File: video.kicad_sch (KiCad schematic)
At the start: 0 parts

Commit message: add video padding circuit
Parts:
- added C46: 180pF, Capacitor_THT:C_Disc_D3.0mm_W2.0mm_P2.50mm, symbol Device:C_Small
- added C47, C71: 100pF, Capacitor_THT:C_Disc_D3.0mm_W2.0mm_P2.50mm, symbol Device:C_Small
- added C73, C99: 180pF, Capacitor_THT:C_Disc_D4.7mm_W2.5mm_P5.00mm, symbol Device:C_Small
- added IC11: MC14053, Package_DIP:DIP-16_W7.62mm, symbol vdg:MC14053
- added IC14: 74LS86AN, Package_DIP:DIP-14_W7.62mm, symbol 74xx:74LS86
- added IC21: 74LS74, Package_DIP:DIP-14_W7.62mm, symbol 74xx:74LS74
- added IC22: 74LS00N, Package_DIP:DIP-14_W7.62mm, symbol 74xx:74LS00
- added IC23: 74ALS74N, Package_DIP:DIP-14_W7.62mm, symbol 74xx:74LS74
- added IC27: 74LS20N, Package_DIP:DIP-14_W7.62mm, symbol 74xx:74LS20
- added IC28, IC29: 74LS393N, Package_DIP:DIP-14_W7.62mm, symbol 74xx:74LS393
- added IC30: 74LS32N, Package_DIP:DIP-14_W7.62mm, symbol 74xx:74LS32
- added IC32: 74LS390, Package_DIP:DIP-16_W7.62mm, symbol 74xx:74LS390
- added IC44: MC3346, Package_DIP:DIP-14_W7.62mm, symbol vdg:MC3346
- added L5, L99: 3.3uH, Inductor_THT:L_Axial_L7.0mm_D3.3mm_P12.70mm_Horizontal_Fastron_MICC, symbol Device:FerriteBead_Small
- added R33: 1K8, Dragon:R_Axial_DIN0309_L9.0mm_D2.5mm_P12.70mm_Horizontal, symbol Device:R_Small
- added R34: 8K2, Dragon:R_Axial_DIN0309_L9.0mm_D2.5mm_P12.70mm_Horizontal, symbol Device:R_Small
- added R35, R92, R94, R99: 12K, Dragon:R_Axial_DIN0309_L9.0mm_D2.5mm_P12.70mm_Horizontal, symbol Device:R_Small
- added U1: LINE_PULSE_DIAGRAM, symbol Dragon32_MKII:LINE_PULSE_DIAGRAM
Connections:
- new net: C46.1, IC30.11, IC30.4
- new net: IC29.11 (Q0), IC30.12
- new net: IC27.12, IC29.10 (Q1), IC30.13
- new net: IC14.6, IC23.11 (C)
- new net: IC14.8, IC23.12 (D)
- new net: IC22.12, IC23.9 (Q)
- new net: IC27.9, IC29.8 (Q3), IC30.10
- new net: C47.1, IC30.5, IC30.8
- new net: IC27.10, IC29.9 (Q2), IC30.9
- new net: IC32.12 (~{CP1}), IC32.7 (Q3)
- new net: C99.2, L99.1
- new net: IC14.11, IC27.1, IC27.2
- new net: IC27.4, IC28.11 (Q0)
- new net: IC27.5, IC28.13 (CP), IC28.6 (Q3)
- new net: IC14.10, IC32.13 (Q0)
- new net: IC32.15 (~{CP0}), IC32.9 (Q3)
- new net: IC22.4, IC22.5, IC27.8
- new net: IC44.5, IC44.8
- new net: IC23.2 (D), IC23.6 (~{Q})
- new net: IC27.13, IC29.5 (Q2)
- new net: IC22.3, R35.2
- new net +5V: IC11.16 (VDD), IC14.13, IC14.14 (VCC), IC14.4, IC21.1 (~{R}), IC21.10 (~{S}), IC21.13 (~{R}), IC21.14 (VCC), IC22.14 (VCC), IC23.1 (~{R}), IC23.10 (~{S}), IC23.13 (~{R}), IC23.14 (VCC), IC23.4 (~{S}), IC27.14 (VCC), IC28.7 (GND), IC29.14 (VCC), IC30.14 (VCC), IC32.16 (VCC), IC44.1, R34.2
- new net CHROME CONTROL: IC23.5 (Q)
- new net CLK: IC22.11
- new net E: IC21.11 (C), IC21.3 (C)
- new net FS': IC14.9, IC27.6
- new net GND: C46.2, C47.2, C71.2, IC11.7 (VEE), IC11.8 (VSS), IC14.7 (GND), IC21.2 (D), IC21.7 (GND), IC22.7 (GND), IC23.7 (GND), IC27.7 (GND), IC28.14 (VCC), IC29.7 (GND), IC30.1, IC30.2, IC30.7 (GND), IC32.14 (MR), IC32.2 (MR), IC32.8 (GND), L99.2, R33.1
- new net LINE PULSE: R33.2, R34.1, R35.1
- new net LINE PULSES: IC14.2, IC22.1, IC22.2, IC30.6, IC32.4 (~{CP1})
- new net LUM CONTROL: IC22.9, IC23.8 (~{Q})
- new net VCLK: IC14.5, IC22.10, IC22.13
- new net u1: IC21.5 (Q), IC22.6, IC29.12 (MR), IC29.2 (MR)
- new net u2: C73.2, IC44.2
- new net u3: IC44.3, R94.2
- new net u4: IC44.4, R92.2
- new net u5: IC44.6, L5.1
- new net u6: C71.1, IC11.14 (X), IC44.10, IC44.13, IC44.7, R99.1
- new net u7: IC44.12
- new net u8: C99.1, IC44.14
- new net ~{FS}: IC14.12, IC21.4 (~{S}), IC28.12 (MR), IC28.2 (MR)
- new net ~{HS}: IC14.1, IC21.12 (D), IC28.1 (CP)
- new net ~{NHS}: IC14.3, IC21.9 (Q), IC23.3 (C)
- new net ~{VCLK}: IC22.8, IC29.1 (CP)
- new net ~{VCLK}/16: IC29.13 (CP), IC29.6 (Q3)
- no-connect marks 0 -> 17
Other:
- note added: "24 LINE DELAY"
- note added: "DIVIDE BY 50"
- note added: "DIVIDE VCLK BY 228 TO CREATE LINE PULSE FREQUENCY"
- note added: "HSYNC DIVIDED BY 2"
- note added: "OUTPUT LOW ON COUNT 0-15 LINE PULSE WIDTH = 4.5us"
- note added: "STEER VCLK TO VDG OR LINE PULSE CIRCUIT"

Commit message: video circuit tracing
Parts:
- added C53, C54, C55, C56: 100nF, Capacitor_THT:C_Disc_D4.3mm_W1.9mm_P5.00mm, symbol Device:C_Small
- added C60: 180pF, Capacitor_THT:C_Disc_D3.0mm_W2.0mm_P2.50mm, symbol Device:C_Small
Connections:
- net +5V: now also IC14.10, IC14.5, IC28.14 (VCC), C53.2, C54.2, C55.2, C56.2; no longer IC14.13, IC14.4, IC28.7 (GND)
- net FS': now also IC14.12; no longer IC14.9
- net GND: now also IC28.7 (GND), C53.1, C54.1, C55.1, C56.1, C60.2; no longer IC28.14 (VCC)
- net LINE PULSE: now also IC11.3 (Z1)
- net LINE PULSES: now also C60.1
- net LUM CONTROL: now also IC11.9 (C)
- net VCLK: now also IC14.4; no longer IC14.5
- net ~{FS}: now also IC14.9; no longer IC14.12
- net at IC23.12 (D): now also IC14.11; no longer IC14.8
- net LUMA': now reaches IC11.4 (Z)
- net LUM: now reaches IC11.5 (Z0)
- net at IC27.1, IC27.2: now also IC14.8; no longer IC14.11
- net at IC32.13 (Q0): now also IC14.13; no longer IC14.10

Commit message: FM generator routing
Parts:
- added C49: 100nF, Capacitor_THT:C_Disc_D4.3mm_W1.9mm_P5.00mm, symbol Device:C_Small
- added C67, C72, C75, C76: 100pF, Capacitor_THT:C_Disc_D3.0mm_W2.0mm_P2.50mm, symbol Device:C_Small
- added C74: 100nF, Capacitor_THT:C_Disc_D4.7mm_W2.5mm_P5.00mm, symbol Device:C_Small
- added C98: 33nF, Capacitor_THT:C_Disc_D3.0mm_W2.0mm_P2.50mm, symbol Device:C_Small
- added DL1: 390ns 1K1, Dragon:Delay_Line-V9663, symbol Device:DelayLine
- added L4: 22uH, Inductor_THT:L_Axial_L9.5mm_D4.0mm_P15.24mm_Horizontal_Fastron_SMCC, symbol Device:FerriteBead_Small
- added L6, L7: 10.7MHz, Dragon:TOKO_RCL_10K, symbol vdg:TOKO_Variable_Inductor
- added R100, R91, R93: 6K5, Dragon:R_Axial_DIN0309_L9.0mm_D2.5mm_P12.70mm_Horizontal, symbol Device:R_Small
- added R77: 1200uH, Dragon:R_Axial_DIN0309_L9.0mm_D2.5mm_P12.70mm_Horizontal, symbol Device:R_Small
- added R86, R96: 47K, Dragon:R_Axial_DIN0309_L9.0mm_D2.5mm_P12.70mm_Horizontal, symbol Device:R_Small
- added R95, R98: 470uH, Dragon:R_Axial_DIN0309_L9.0mm_D2.5mm_P12.70mm_Horizontal, symbol Device:R_Small
- added R97: 270R, Dragon:R_Axial_DIN0309_L9.0mm_D2.5mm_P12.70mm_Horizontal, symbol Device:R_Small
- C73: value 180pF -> 100nF
- L5: footprint Inductor_THT:L_Axial_L7.0mm_D3.3mm_P12.70mm_Horizontal_Fastron_MICC -> Inductor_THT:L_Axial_L9.5mm_D4.0mm_P15.24mm_Horizontal_Fastron_SMCC
- R92: value 12K -> 6K5
- R94, R99: value 12K -> 1K6
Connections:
- net +5V: now also IC44.11, C49.2, L6.1
- net CHROME CONTROL: now also IC11.10 (B)
- net E: now also IC30.2
- net GND: now also C46.1, C47.1, IC11.6 (INHIBIT), R94.1, R99.2, C49.1, C74.1, DL1.3 (COMMUN), L6.5 (GND), L7.5 (GND), R100.2, R91.1; no longer C46.2, C47.2, C71.2, IC30.1, IC30.2
- net u2: now also C72.1
- net u4: now also C74.2, R93.2, R95.1
- net u6: no longer IC11.14 (X)
- net ~{NHS}: no longer IC14.3, IC23.3 (C)
- net at IC30.11, IC30.4: now also C46.2; no longer C46.1
- net at C73.1: now also R92.1
- net at IC30.5, IC30.8: now also C47.2; no longer C47.1
- net C1: now reaches IC11.2 (Y0)
- net C1: now also R86.2
- net DA0': now reaches IC30.3
- net u9: now reaches IC44.5, IC44.8
- net u9: now also C71.2, C72.2, C75.2, L6.3
- net u10: now reaches IC44.9
- net u10: now also IC11.14 (X)
- net u1: no longer names the net of IC22.6, IC29.12 (MR), IC29.2 (MR)
- net u1: no longer IC21.5 (Q)
- new net: C67.1, R86.1
- new net: C76.2, R100.1
- new net: C98.1, R77.1, R95.2
- new net: R93.1, R96.1
- new net: L7.1, R98.1
- new net: C76.1, L7.3
- new net: C98.2, L4.2
- new net: C75.1, R91.2
- new net: IC14.3, IC23.3 (C)
- new net DA0: IC30.1
- new net ~{NFS}: IC21.5 (Q)
- no-connect marks 17 -> 19
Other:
- moved on the sheet: C71, C73, C99, IC11, IC14A, IC21A, IC21B, IC23A, IC28B, IC30A, L5, L99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

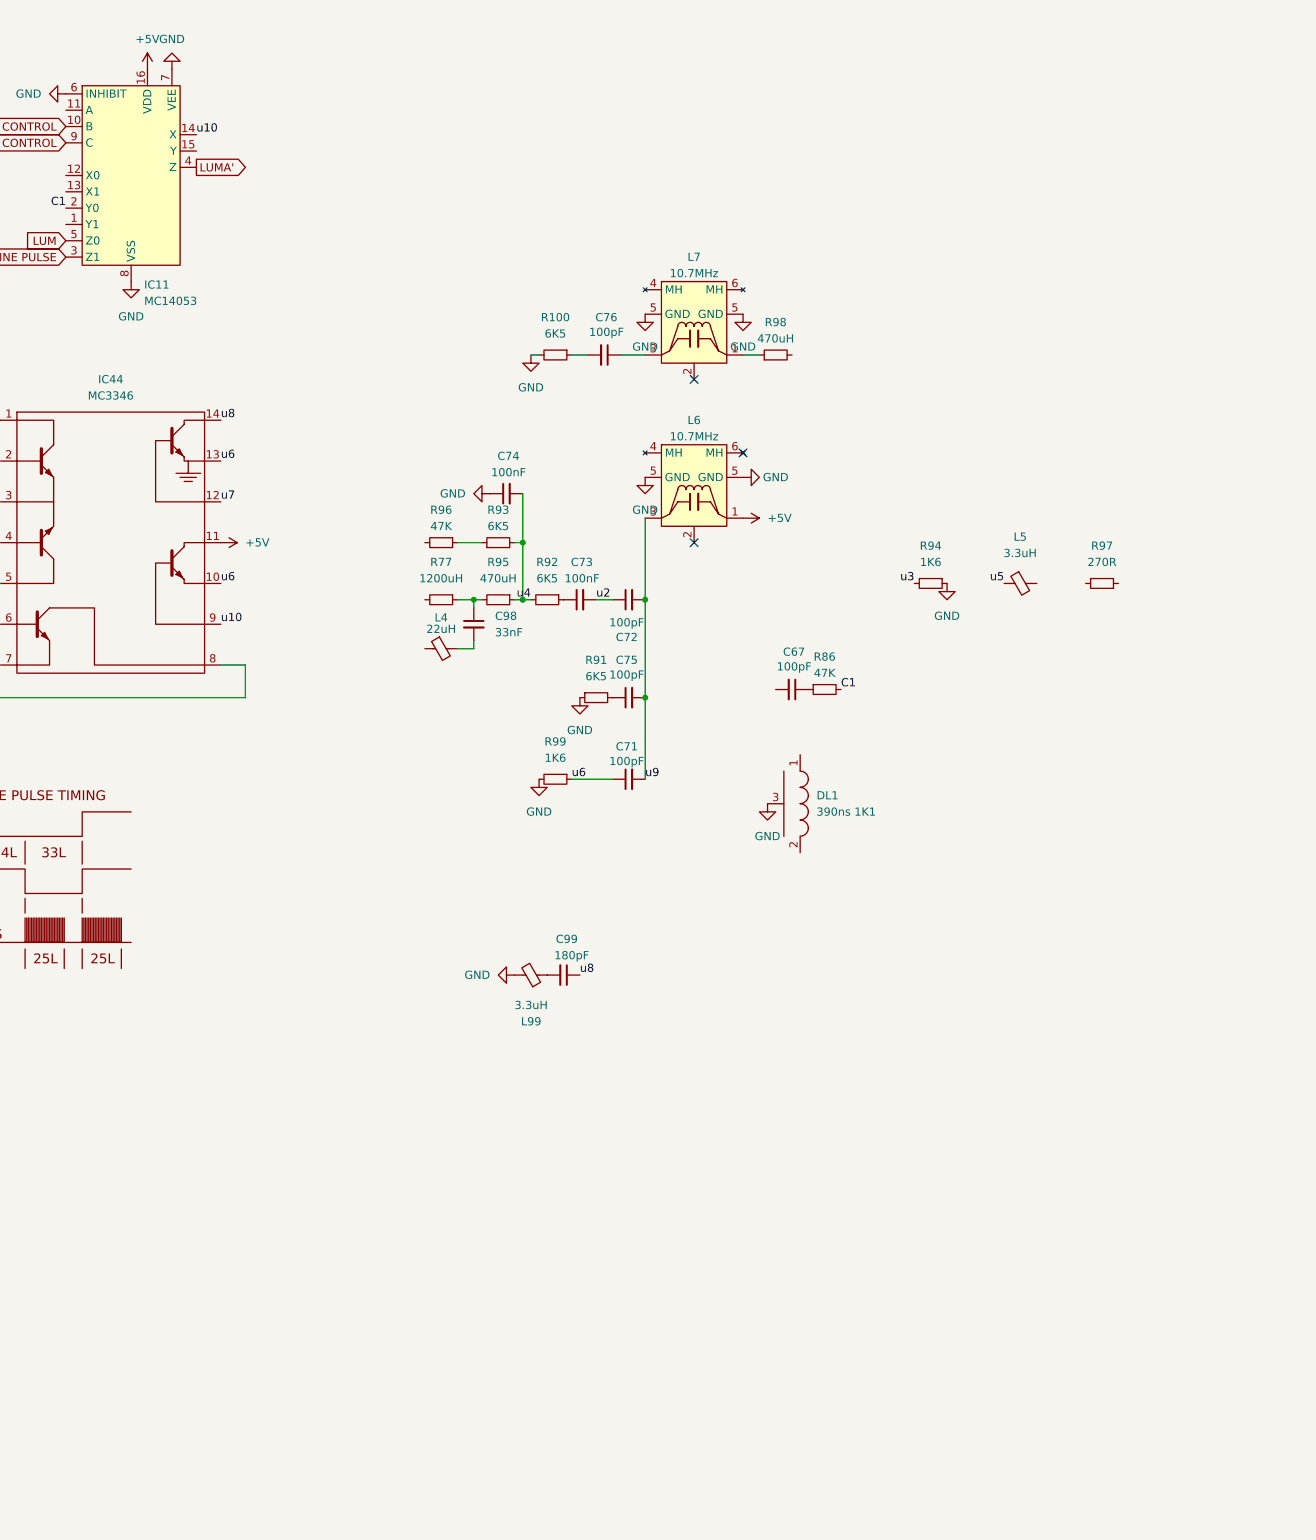
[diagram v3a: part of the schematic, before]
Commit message: complete physical layout
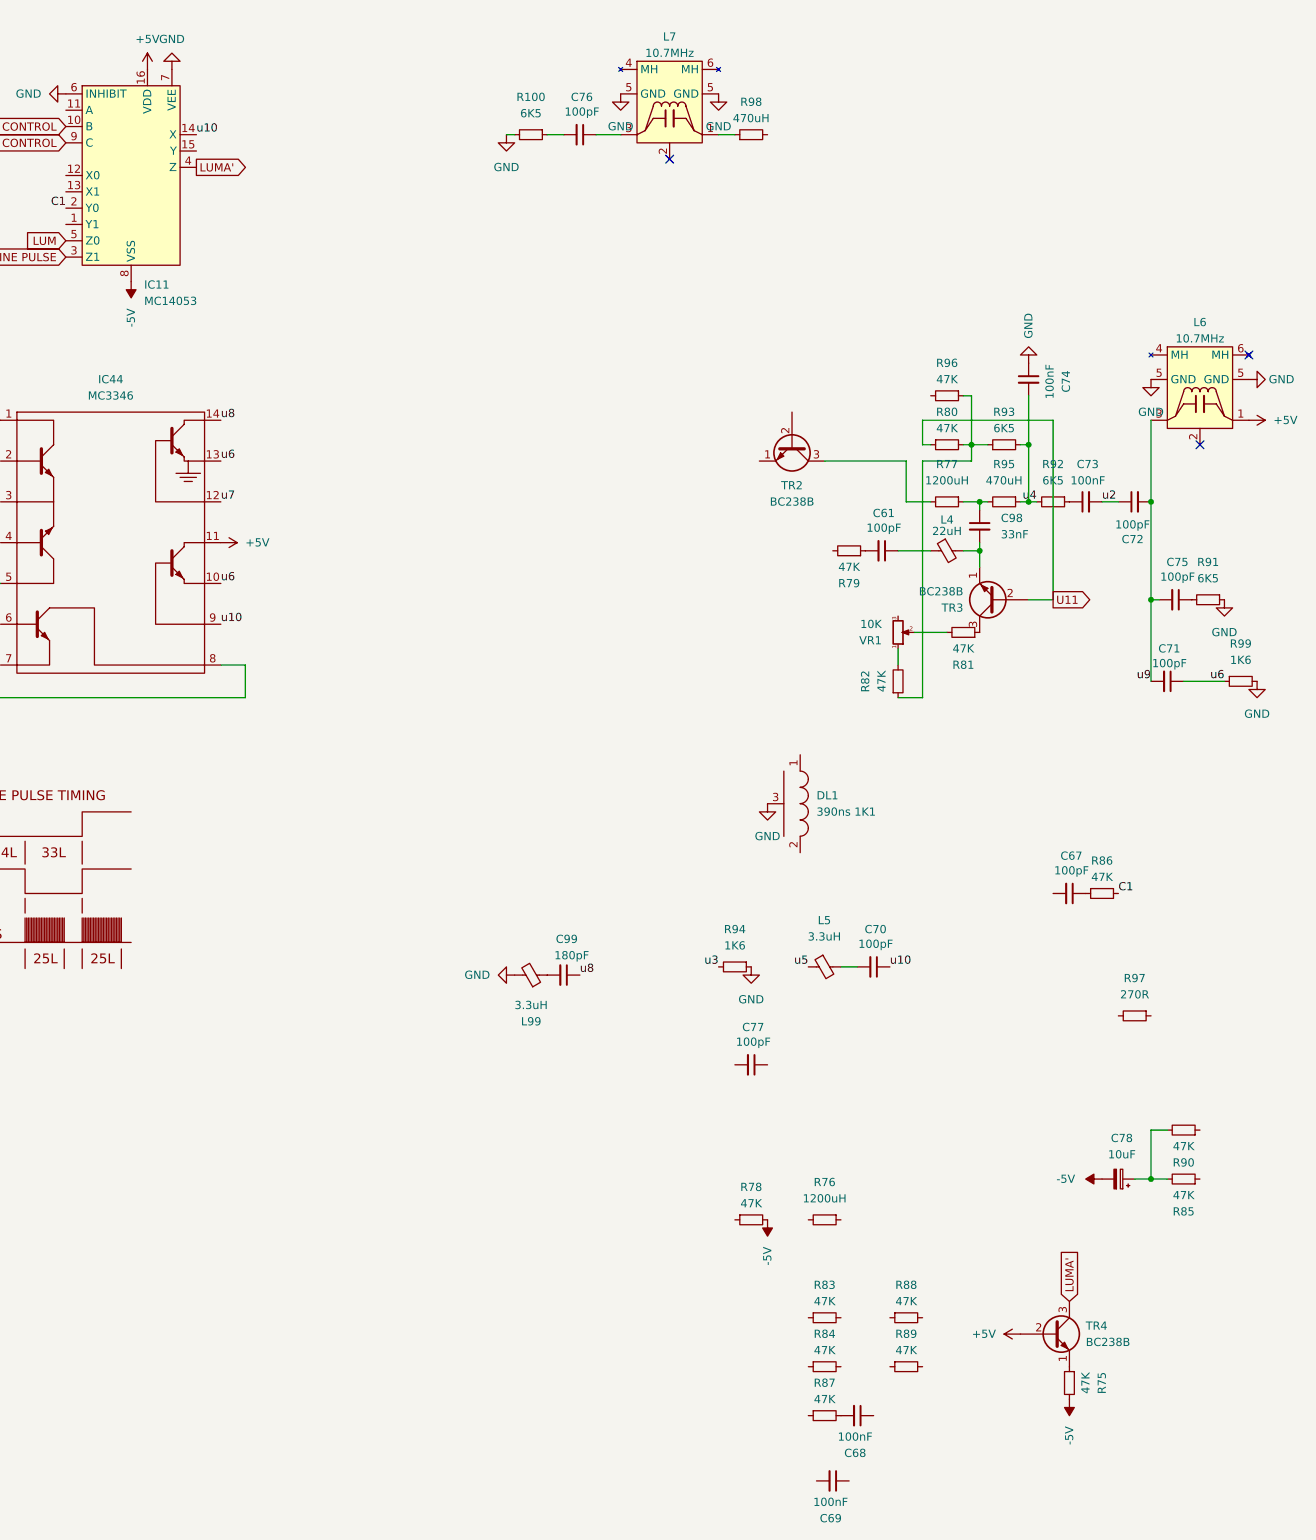
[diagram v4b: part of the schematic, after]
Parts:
- added C61, C70, C77: 100pF, Capacitor_THT:C_Disc_D3.0mm_W2.0mm_P2.50mm, symbol Device:C_Small
- added C68, C69: 100nF, Capacitor_THT:C_Disc_D4.7mm_W2.5mm_P5.00mm, symbol Device:C_Small
- added C78: 10uF, Capacitor_THT:CP_Radial_D8.0mm_P5.00mm, symbol Device:C_Polarized_Small
- added R75, R78, R79, R80, R81, R82, R83, R84, R85, R87, R88, R89, R90: 47K, Dragon:R_Axial_DIN0309_L9.0mm_D2.5mm_P12.70mm_Horizontal, symbol Device:R_Small
- added R76: 1200uH, Dragon:R_Axial_DIN0309_L9.0mm_D2.5mm_P12.70mm_Horizontal, symbol Device:R_Small
- added TR2, TR3, TR4: BC238B, Package_TO_SOT_THT:TO-92, symbol Device:Q_NPN_EBC
- added VR1: 10K, Potentiometer_THT:Potentiometer_ACP_CA6-H2,5_Horizontal, symbol Device:R_Potentiometer_Small
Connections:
- net +5V: now also TR4.2 (B)
- net GND: no longer IC11.8 (VSS)
- net LUMA': now also TR4.3 (C)
- net u10: now also C70.1
- net at R77.2: now also TR2.3 (C)
- net at L5.2: now also C70.2
- net at R93.1, R96.1: now also R80.2, R82.1
- net at C98.2, L4.2: now also TR3.1 (E)
- net at L4.1: now also C61.1
- new net: C68.2, R87.2
- new net: R81.1, TR3.3 (C)
- new net: R81.2, VR1.2
- new net: C61.2, R79.1
- new net: R75.1, TR4.1 (E)
- new net: C78.1, R85.2, R90.2
- new net: R82.2, VR1.1
- new net -5V: C78.2, IC11.8 (VSS), R75.2, R78.2
- new net U11: R80.1, TR3.2 (B)
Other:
- moved on the sheet: C67, C71, C72, C73, C74, C75, C76, C98, L4, L5, L6, L7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

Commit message: fm circuit routing
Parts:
- added C65: 100pF, Capacitor_THT:C_Disc_D3.0mm_W2.0mm_P2.50mm, symbol Device:C_Small
- R89: value 47K -> 1200uH
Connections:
- net -5V: now also IC11.7 (VEE); no longer IC11.8 (VSS)
- net CHROME CONTROL: now also C68.1
- net GND: now also C69.2, IC11.8 (VSS); no longer IC11.7 (VEE)
- net u12: now reaches R87.1
- net u12: now also C69.1, IC11.1 (Y1), IC11.12 (X0), R89.1
- net at R77.2, TR2.3 (C): now also DL1.2
- net at R88.1: now also R89.2
- net u13: now reaches R88.2
- net u13: now also IC11.13 (X1), R83.2, R84.2
- net at R75.1, TR4.1 (E): now also R76.1
- net at R84.1: now also C65.1
- net at R76.2: now also DL1.1
- net phiA: now reaches C67.2
- net phiA: now also R85.1
- net phiB: now reaches R83.1
- net phiB: now also C65.2
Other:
- moved on the sheet: C68, C69, DL1, R75, R76, R78, R84, R87, R88, R89, TR2, TR4

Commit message: trace work complete
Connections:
- net +5V: now also R97.2, TR2.2 (B)
- net -5V: no longer C78.2
- net C1: now also R85.2, R90.1
- net CHROME CONTROL: now also IC11.11 (A)
- net GND: now also C78.2
- net u6: now also R98.2
- net u8: now also C77.2, R97.1
- net at R81.1, TR3.3 (C): now also C77.1
- net at C61.2, R79.1: now also R78.1, TR2.1 (E)
- net at R79.2: now also C61.1, L4.1
- net at R88.1, R89.2: now also C78.1, R90.2
- net LUMA'2: now reaches R75.1, R76.1, TR4.1 (E)
- no-connect marks 19 -> 20
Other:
- moved on the sheet: C61, C67, C68, C69, C77, C78, R78, R79, R85, R86, R87, R88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

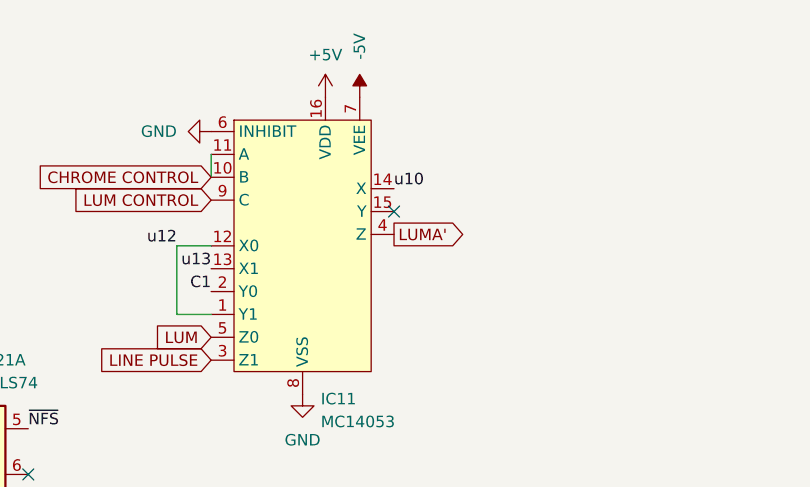
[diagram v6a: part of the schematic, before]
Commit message: attach u5 to 4053-pin 15 (B control)
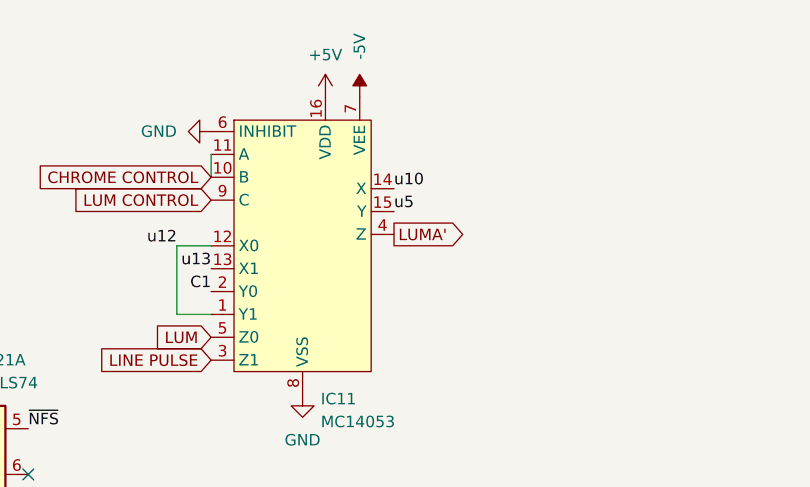
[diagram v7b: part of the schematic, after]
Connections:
- net u5: now also IC11.15 (Y)
- no-connect marks 20 -> 19
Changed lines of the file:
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@@
-	)
-	(no_connect
-		(at 262.89 33.02)
 	)
 	(no_connect
@@
 		)
 	)
+	(label "u5"
+		(at 262.89 33.02 0)
+		(effects
+			(font
+				(size 1.27 1.27)
+			)
+			(justify left bottom)
+		)
+	)
